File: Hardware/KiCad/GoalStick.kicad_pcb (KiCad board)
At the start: 2 copper layers, 134.6 x 81.3 mm, 6 parts, among them J1 Barrel_Jack_Switch

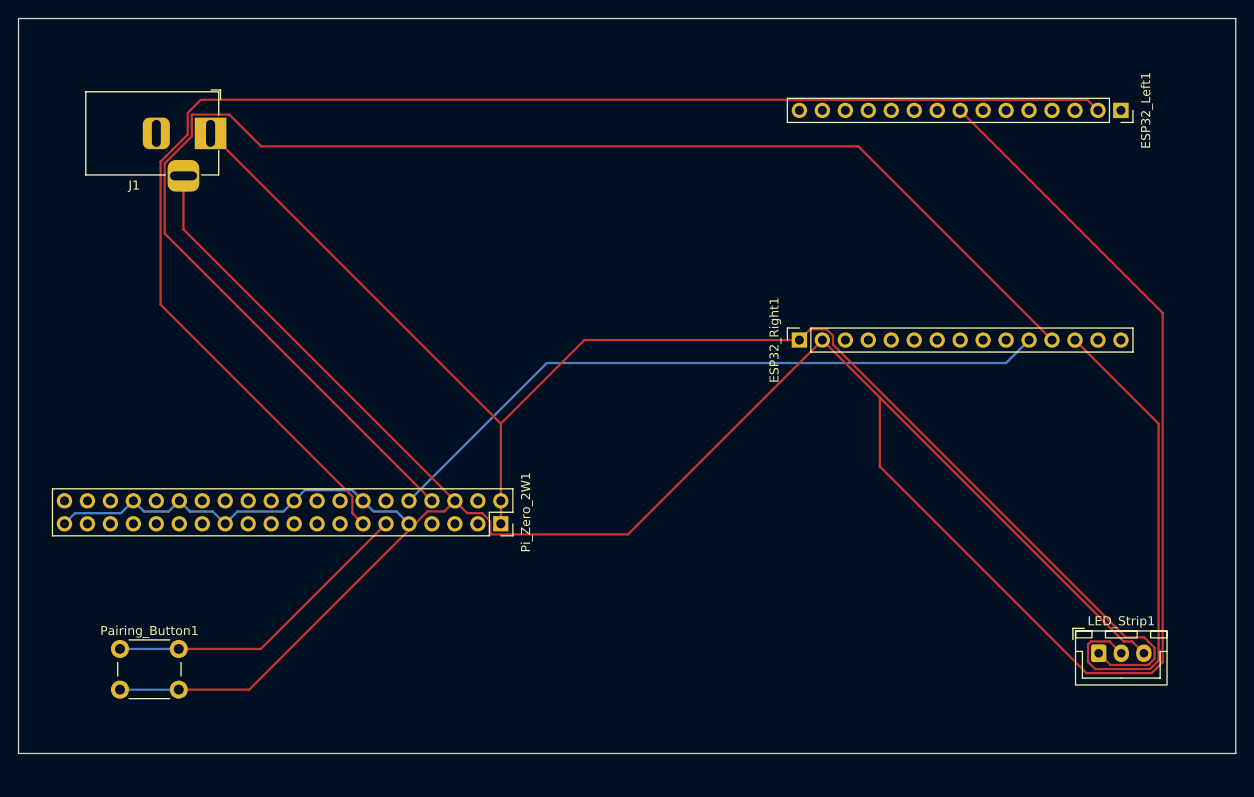
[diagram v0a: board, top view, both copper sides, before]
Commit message: Add DEPLOYMENT.md, update ESP32 firmware for XIAO ESP32C3, add KiCad footprints
- Add DEPLOYMENT.md with hands-free installation instructions
- Update README.md to link to deployment guide
- Update ESP32 firmware for XIAO ESP32C3 (Serial1, pin mappings, startup delay)
- Add custom KiCad footprints for XIAO and Pi Zero 2W
- Update KiCad schematic and PCB layout
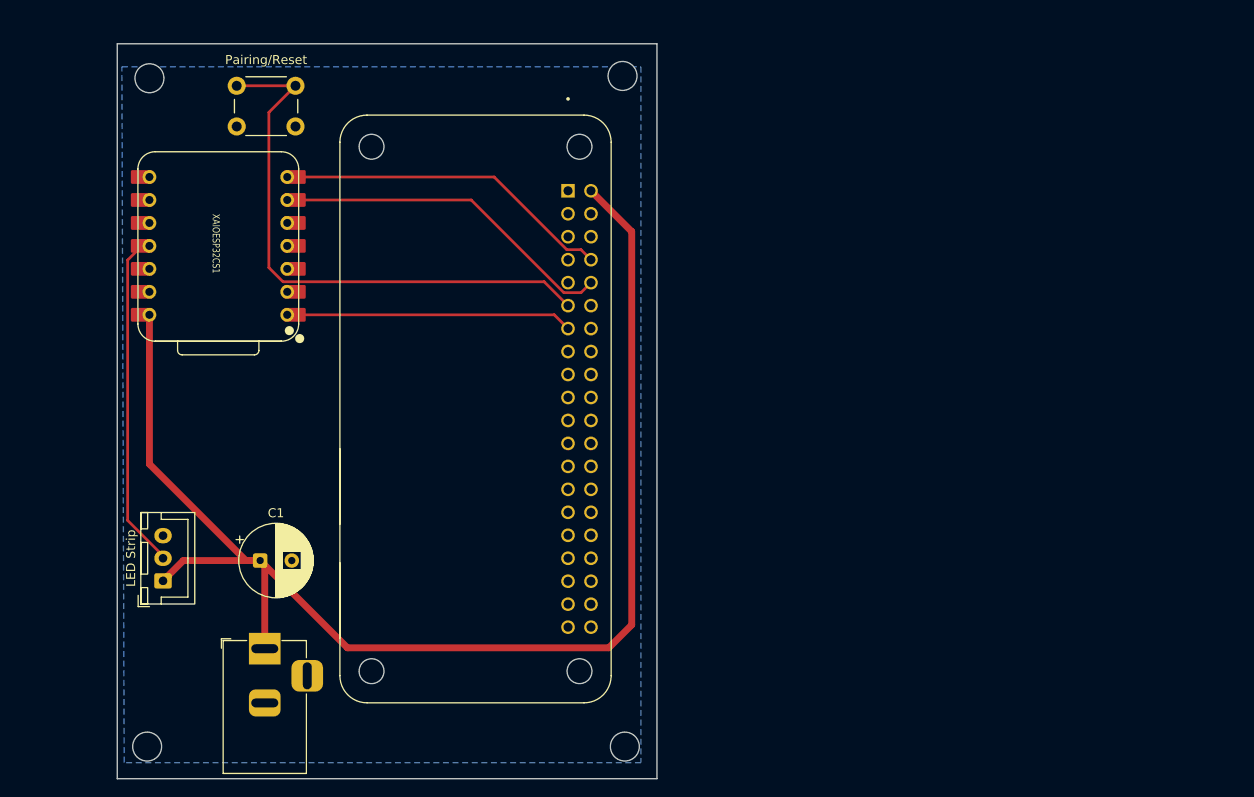
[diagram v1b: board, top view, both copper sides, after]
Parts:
- removed ESP32_Left1, ESP32_Right1: Conn_01x15, Connector_PinSocket_2.54mm:PinSocket_1x15_P2.54mm_Vertical
- removed LED_Strip1: Conn_01x03, Connector_JST:JST_XH_B3B-XH-A_1x03_P2.50mm_Vertical
- removed Pairing_Button1: SW_Push, Button_Switch_THT:SW_PUSH_6mm
- removed Pi_Zero_2W1: Conn_02x20_Counter_Clockwise, Connector_PinSocket_2.54mm:PinSocket_2x20_P2.54mm_Vertical
- added C1: C_Polarized, Capacitor_THT:CP_Radial_D8.0mm_P3.50mm, F.Cu at (44.5, 77.7)
- added LED Strip: Conn_01x03, Connector_JST:JST_XH_B3B-XH-A_1x03_P2.50mm_Vertical, F.Cu at (33.8, 80.0)
- added Mount: MountingHole_3.2mm_M3, MountingHole:MountingHole_3.2mm_M3, F.Cu at (84.6, 24.1)
- added Pairing/Reset: SW_Push, Button_Switch_THT:SW_PUSH_6mm, F.Cu at (41.9, 25.2)
- added REF**: MountingHole_3.2mm_M3, MountingHole:MountingHole_3.2mm_M3, F.Cu at (84.8, 98.3)
- added REF**: MountingHole_3.2mm_M3, MountingHole:MountingHole_3.2mm_M3, F.Cu at (32.3, 24.4)
- added REF**: MountingHole_3.2mm_M3, MountingHole:MountingHole_3.2mm_M3, F.Cu at (32.0, 98.3)
- added U2: RASPBERRY_PI_ZERO_2_W, RASPBERRY_PI_ZERO_2_W:MODULE_RASPBERRY_PI_ZERO_2_W, F.Cu at (68.3, 61.0)
- added XAIOESP32CS1: ~, XAIO_Series:XIAO-ESP32-C3-DIP, F.Cu at (39.9, 42.9)
- J1: value Barrel_Jack_Switch -> Power Barrel Jack
- moved J1 57.3 mm to (45.0, 87.5), turned to 90 degrees
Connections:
- J1 pad 1: +5V -> /+5V
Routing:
- net GND: track 359.4 -> 0.00 mm
- net +5V: track 156.5 -> 0.00 mm
- net /+5V: track 0.00 -> 150.8 mm
- net /ESP_RESET: track 157.7 -> 31.7 mm
- net /UART_TX: track 161.7 -> 38.3 mm
- net /UART_RX: track 75.9 -> 37.4 mm
- net /BTN: track 35.2 -> 62.7 mm
- net /LED_DATA: track 54.1 -> 36.8 mm
- added copper zone on B.Cu, net GND
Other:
- board size 134.6 x 81.3 mm -> 59.7 x 81.3 mm

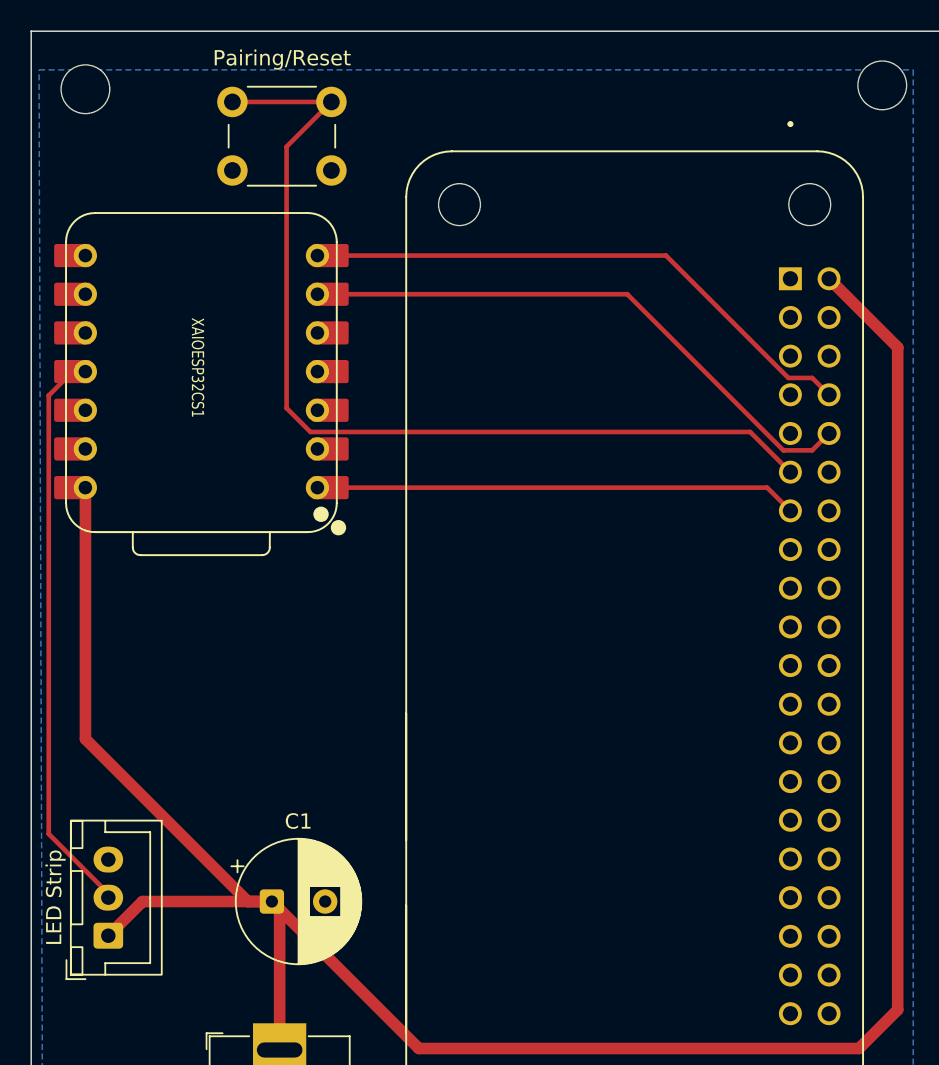
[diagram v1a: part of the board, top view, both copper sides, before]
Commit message: Update .gitignore and remove generated/local KiCad files from repo
Fixed bad routes on the Pi to ESP32 serial connections, updated SMD pads on the ESP32 to drilled holes.
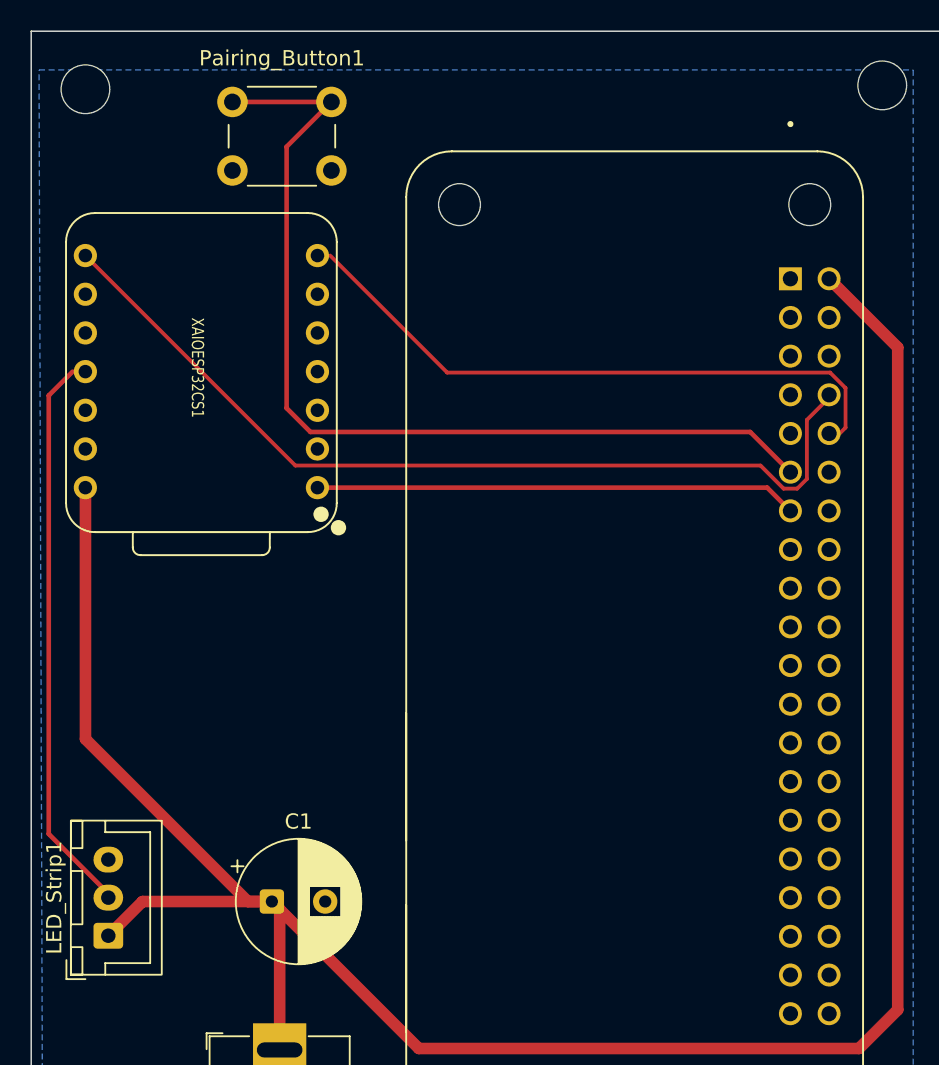
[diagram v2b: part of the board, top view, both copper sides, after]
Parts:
- J1: value Power Barrel Jack -> Barrel_Jack_Switch
- LED_Strip1: renamed from LED Strip
- renumbered Pairing/Reset to Pairing_Button1
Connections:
- U2 pad 10: /UART_TX -> /UART_RX
- U2 pad 8: /UART_RX -> /UART_TX
- XAIOESP32CS1 pad 6: /UART_TX -> unconnected-(XAIOESP32CS1-D5-Pad6)
- XAIOESP32CS1 pad 8: unconnected-(XAIOESP32CS1-D7-Pad8) -> /UART_TX
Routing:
- net /UART_TX: track 38.3 -> 60.4 mm
- net /UART_RX: track 37.4 -> 41.5 mm
